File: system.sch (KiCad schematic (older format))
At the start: 23 parts, among them IC2 AM335X_ZCZ, P5 JTAG, U4 74LVC1G07DCK, Y1 24MHz, Y2 32.768kHz MC-306

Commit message: add display connector, bom generated, sch second version
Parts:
- added L11: BLM15AG102SN1D, symbol L
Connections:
- net labels added: CLKOUT1
- wire segments 61 -> 62
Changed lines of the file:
@@
 JTAG_EMU1
 Wire Wire Line
-	5725 4275 6200 4275
+	5725 4275 6350 4275
 Text Label 6200 4275 2    60   ~ 0
 JTAG_EMU2
@@
 P 5725 4575
 F 0 "W2" V 5725 4800 50  0000 C CNN
-F 1 "TESTOUT" V 5725 5075 50  0000 C CNN
+F 1 "TESTOUT" V 5800 4900 50  0000 C CNN
 F 2 "" H 5925 4575 50  0000 C CNN
 F 3 "" H 5925 4575 50  0000 C CNN
@@
 U 1 1 58B9CB53
 P 6500 4375
-F 0 "L8" V 6450 4375 50  0000 C CNN
-F 1 "BLM15AG102SN1D" V 6575 4375 50  0000 C CNN
+F 0 "L8" V 6575 4375 50  0000 C CNN
+F 1 "BLM15AG102SN1D" V 6650 4375 50  0000 C CNN
 F 2 "" H 6500 4375 50  0001 C CNN
 F 3 "" H 6500 4375 50  0001 C CNN
@@
 Wire Wire Line
 	6900 4375 6650 4375
+Text HLabel 6900 4275 2    60   Output ~ 0
+CLKOUT1
+$Comp
+L L L11
+U 1 1 58CCCA16
+P 6500 4275
+F 0 "L11" V 6375 4275 50  0000 C CNN
+F 1 "BLM15AG102SN1D" V 6450 4325 50  0000 C CNN
+F 2 "" H 6500 4275 50  0001 C CNN
+F 3 "" H 6500 4275 50  0001 C CNN
+	1    6500 4275
+	0    1    1    0
+$EndComp
+Wire Wire Line
+	6650 4275 6900 4275
 $EndSCHEMATC

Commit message: wip bom, fix some capacitors
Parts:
- C116, C117: value 100nF/10V -> 100nF/6.3V
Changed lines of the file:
@@
 P 2400 6300
 F 0 "C116" H 2425 6400 50  0000 L CNN
-F 1 "100nF/10V" H 2425 6200 50  0000 L CNN
+F 1 "100nF/6.3V" H 2425 6200 50  0000 L CNN
 F 2 "" H 2438 6150 50  0000 C CNN
 F 3 "" H 2400 6300 50  0000 C CNN
@@
 P 3325 6550
 F 0 "C117" H 3350 6650 50  0000 L CNN
-F 1 "100nF/10V" H 3350 6450 50  0000 L CNN
+F 1 "100nF/6.3V" H 3350 6450 50  0000 L CNN
 F 2 "" H 3363 6400 50  0000 C CNN
 F 3 "" H 3325 6550 50  0000 C CNN

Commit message: wip sch
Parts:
- removed C120, C121: 18pF/50V, symbol C
- removed IC2: AM335X_ZCZ, symbol AM335X_ZCZ
- removed Y2: 32.768kHz MC-306, symbol Crystal_GND23
- added C? (x2): 18pF/50V, symbol C
- added C?: 2.2uF/6.3V, symbol C
- added C?: 100nF/6.3V, symbol C
- added D? (x4): LTST-C191TBKT, symbol LED
- added IC?: OSD335x, GHI-SoMs-Processors_OSD3358, symbol OSD335x
- added IC?: NAND_4GB, footprints:WFBGA153, symbol NAND_4GB
- added P?: microSD, symbol microSD
- added R?: DNP 1M, symbol R
- added R? (x4): 1k, symbol R
- added R? (x18): 10k, symbol R
- added R?: 0R, symbol R
- added U?: SN74LVC1G06DCK, symbol 74AHC1G14
- added Y?: 32.768kHz, symbol Crystal
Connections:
- net labels added: GNDSHIELD, MMC1_CLK, MMC1_CMD, MMC1_DAT0, MMC1_DAT1, MMC1_DAT2, MMC1_DAT3, MMC1_DAT4, MMC1_DAT5, MMC1_DAT6, MMC1_DAT7, SD.CD, SD.CLK, SD.CMD, SD.D0, SD.D1, SD.D2, SD.D3, TIMER4, TIMER5, TIMER6, TIMER7, USR0, USR1, USR2, USR3, eHRPWM1A, eHRPWM1B, eHRPWM2A, eHRPWM2B, eMMC_RSTn
- net labels removed: GND_OSC, VSS_RTC
- wire segments 62 -> 254
- no-connect marks 3 -> 1
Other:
- moved on the sheet: C116, C117, C118, C119, C122, L11, L8, R32, R33, R34, R35, R36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

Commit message: wip sys and power
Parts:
- removed C116, C117: 100nF/6.3V, symbol C
- removed D? (x4): LTST-C191TBKT, symbol LED
- removed L11: BLM15AG102SN1D, symbol L
- removed P5: JTAG, symbol CONN_02X10
- removed P?: microSD, symbol microSD
- removed R32, R33, R34, R35: 4.75k, symbol R
- removed R37: 0R, symbol R
- removed R38, R? (x7): 10k, symbol R
- removed R? (x4): 1k, symbol R
- removed S2: Reset Button, symbol PushButton
- removed W2: TESTOUT, symbol TEST_1P
- added C? (x3): 100nF/6.3V, symbol C
- added C? (x3): 2.2uF/6.3V, symbol C
- added L?: BLM15AG102SN1D, symbol L
- added R?: 0 1%, symbol R
- added R?: 0R, symbol R
- C122: value 2.2uF/10V -> 2.2uF/6.3V
- C?: value 2.2uF/6.3V -> 4.7uF/6.3V
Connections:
- net labels added: GPIO0_26, GPIO0_27, GPIO1_12, GPIO1_13, GPIO1_14, GPIO1_15, GPIO1_16, GPIO1_25, GPIO1_28, GPIO1_29, GPIO2_0, GPIO2_1, LDO_PGOOD, PMIC_INT, PMIC_PGOOD, PMIC_nWAKEUP, UART4_RXD, UART4_TXD, USB1_OCn, VDD_1V8
- net labels removed: GNDSHIELD, GPIO0_7, JTAG_EMU2, JTAG_EMU3, JTAG_EMU4, NMIn, PMIC_POWER_EN, POR, RTC_POR, VIO, VRTC, WAKEUP
- wire segments 254 -> 151
- no-connect marks 1 -> 0
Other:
- moved on the sheet: C122, C?, IC?, L8, R39, R?, U4, U?

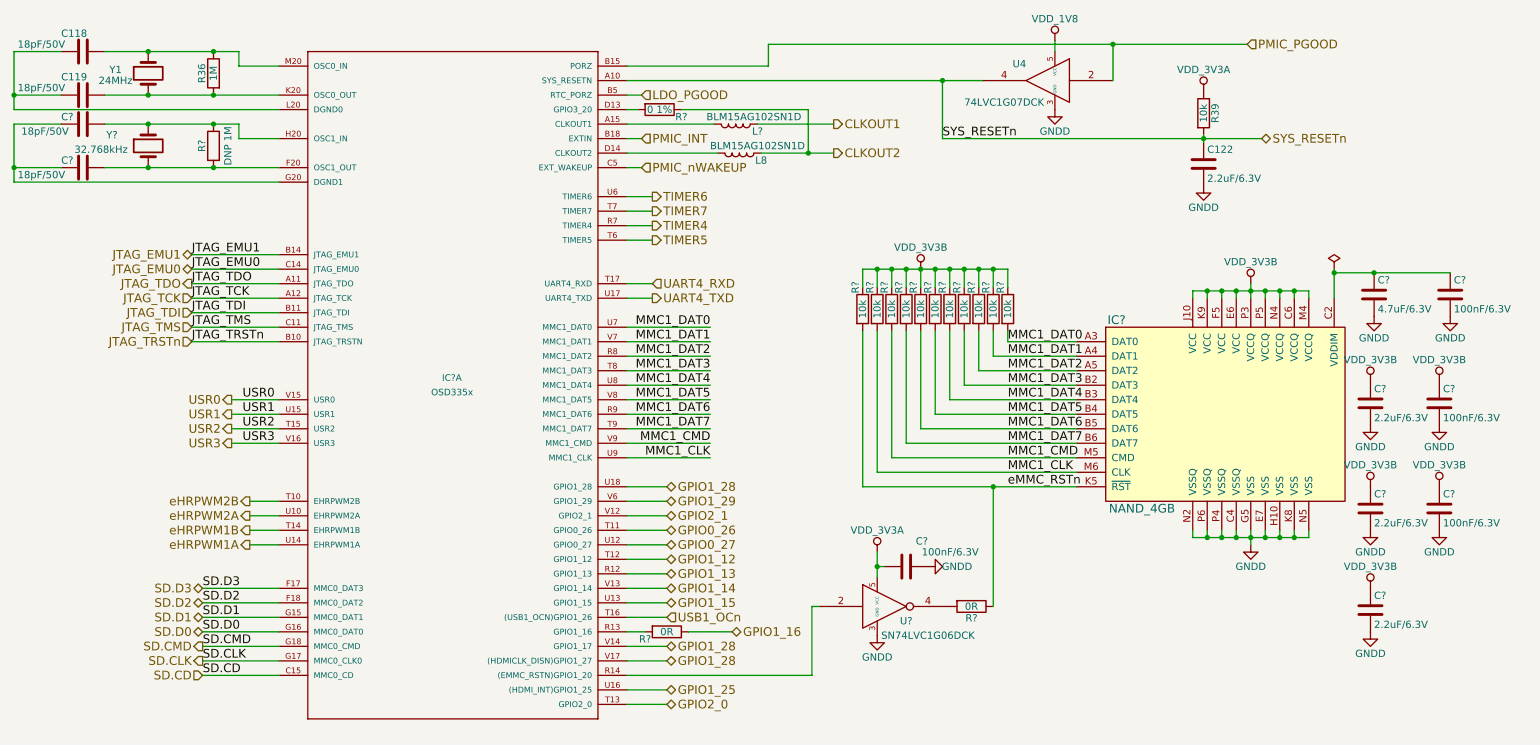
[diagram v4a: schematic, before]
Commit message: only io connectors remaining
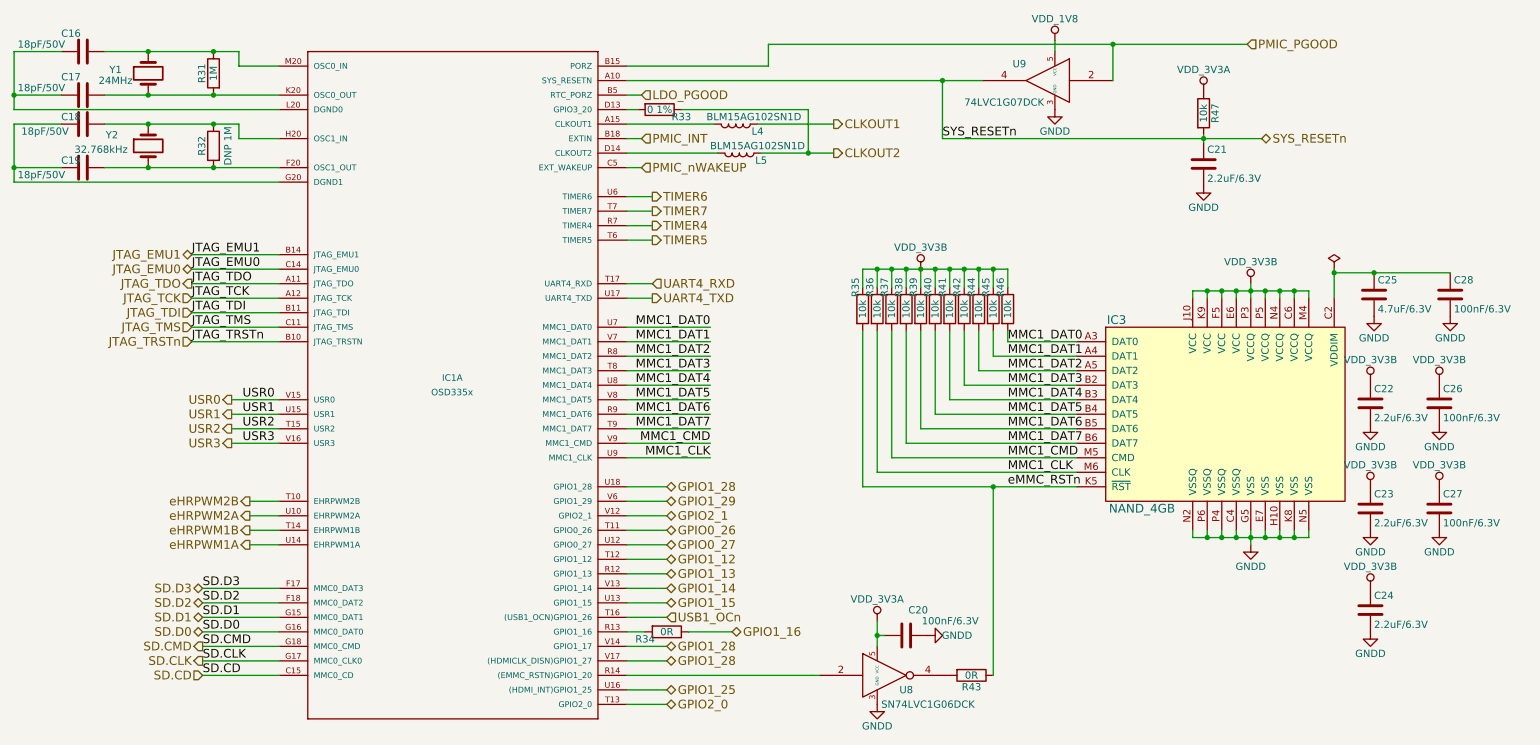
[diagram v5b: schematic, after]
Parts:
- gave numbers to parts that had none: 30
- renumbered C118 to C16, C119 to C17, C122 to C21, L8 to L5, R36 to R31, R39 to R47, U4 to U9
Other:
- moved on the sheet: C20, R43, U8

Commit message: wip erc
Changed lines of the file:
@@
 $EndComp
 Wire Wire Line
-	1375 775  1675 775
-Wire Wire Line
-	1675 775  2125 775
-Wire Wire Line
-	2125 775  2300 775
-Wire Wire Line
-	1375 1075 1675 1075
-Wire Wire Line
-	1675 1075 2125 1075
-Wire Wire Line
-	2125 1075 2575 1075
+	1375 775  2300 775
+Wire Wire Line
+	1375 1075 2575 1075
 $Comp
 L R R31
@@
 	1075 775  750  775
 Wire Wire Line
-	750  775  750  1075
-Wire Wire Line
-	750  1075 750  1175
+	750  775  750  1175
 Wire Wire Line
 	750  1075 1075 1075
@@
 $EndComp
 Wire Wire Line
-	5950 725  8325 725
-Wire Wire Line
-	8325 725  9250 725
+	5950 725  9250 725
 Text HLabel 9250 725  2    60   Input ~ 0
 PMIC_PGOOD
@@
 $EndComp
 Wire Wire Line
-	4975 975  7150 975
-Wire Wire Line
-	7150 975  7425 975
+	4975 975  7425 975
 $Comp
 L GNDD #PWR75
@@
 Connection ~ 8325 725
 Wire Wire Line
-	7150 1375 8950 1375
-Wire Wire Line
-	8950 1375 9350 1375
+	7150 1375 9350 1375
 Wire Wire Line
 	7150 1375 7150 975
@@
 $EndComp
 Wire Wire Line
-	8950 1350 8950 1375
-Wire Wire Line
-	8950 1375 8950 1400
+	8950 1350 8950 1400
 Connection ~ 8950 1375
 $Comp
@@
 CLKOUT2
 Wire Wire Line
-	5900 1475 6225 1475
-Wire Wire Line
-	6225 1475 6400 1475
+	5900 1475 6400 1475
 $Comp
 L OSD335x IC1
@@
 $EndComp
 Wire Wire Line
-	1375 1275 1675 1275
-Wire Wire Line
-	1675 1275 2125 1275
-Wire Wire Line
-	2125 1275 2300 1275
-Wire Wire Line
-	1375 1575 1675 1575
-Wire Wire Line
-	1675 1575 2125 1575
-Wire Wire Line
-	2125 1575 2575 1575
+	1375 1275 2300 1275
+Wire Wire Line
+	1375 1575 2575 1575
 $Comp
 L R R32
@@
 	1075 1275 750  1275
 Wire Wire Line
-	750  1275 750  1575
-Wire Wire Line
-	750  1575 750  1675
+	750  1275 750  1675
 Wire Wire Line
 	750  1575 1075 1575
@@
 Connection ~ 9175 2425
 Wire Wire Line
-	9275 2375 9275 2425
-Wire Wire Line
-	9275 2425 9275 2475
+	9275 2375 9275 2475
 Connection ~ 9275 2425
 Wire Wire Line
@@
 	9675 2425 9675 2475
 Wire Wire Line
-	8875 2425 8975 2425
-Wire Wire Line
-	8975 2425 9075 2425
-Wire Wire Line
-	9075 2425 9175 2425
-Wire Wire Line
-	9175 2425 9275 2425
-Wire Wire Line
-	9275 2425 9375 2425
-Wire Wire Line
-	9375 2425 9475 2425
-Wire Wire Line
-	9475 2425 9575 2425
-Wire Wire Line
-	9575 2425 9675 2425
+	8875 2425 9675 2425
 $Comp
 L C C25
@@
 $EndComp
 Wire Wire Line
-	9850 2275 9850 2300
-Wire Wire Line
-	9850 2300 9850 2475
-Wire Wire Line
-	9850 2300 10125 2300
-Wire Wire Line
-	10125 2300 10650 2300
+	9850 2275 9850 2475
+Wire Wire Line
+	9850 2300 10650 2300
 $Comp
 L GNDD #PWR79
@@
 Connection ~ 9175 4125
 Wire Wire Line
-	9275 4075 9275 4125
-Wire Wire Line
-	9275 4125 9275 4175
+	9275 4075 9275 4175
 Connection ~ 9275 4125
 Wire Wire Line
@@
 	9675 4125 9675 4075
 Wire Wire Line
-	8875 4125 8975 4125
-Wire Wire Line
-	8975 4125 9075 4125
-Wire Wire Line
-	9075 4125 9175 4125
-Wire Wire Line
-	9175 4125 9275 4125
-Wire Wire Line
-	9275 4125 9375 4125
-Wire Wire Line
-	9375 4125 9475 4125
-Wire Wire Line
-	9475 4125 9575 4125
-Wire Wire Line
-	9575 4125 9675 4125
+	8875 4125 9675 4125
 $Comp
 L R R42
@@
 Connection ~ 6900 2275
 Wire Wire Line
-	6600 2275 6700 2275
-Wire Wire Line
-	6700 2275 6800 2275
-Wire Wire Line
-	6800 2275 6900 2275
-Wire Wire Line
-	6900 2275 7000 2275
-Wire Wire Line
-	7000 2275 7100 2275
-Wire Wire Line
-	7100 2275 7200 2275
-Wire Wire Line
-	7200 2275 7300 2275
-Wire Wire Line
-	7300 2275 7400 2275
-Wire Wire Line
-	7400 2275 7500 2275
-Wire Wire Line
-	7500 2275 7600 2275
+	6600 2275 7600 2275
 Wire Wire Line
 	7000 2275 7000 2400
@@
 	6600 2700 6600 3775
 Wire Wire Line
-	6600 3775 7500 3775
-Wire Wire Line
-	7500 3775 8075 3775
+	6600 3775 8075 3775
 Text Label 7600 2775 0    60   ~ 0
 MMC1_DAT0
@@
 	6750 4800 6700 4800
 Wire Wire Line
-	6700 4700 6700 4800
-Wire Wire Line
-	6700 4800 6700 4875
+	6700 4700 6700 4875
 Connection ~ 6700 4800
 Wire Wire Line
@@
 $EndComp
 Wire Wire Line
-	4975 5075 6250 5075
-Wire Wire Line
-	6250 5075 6250 5075
-Wire Wire Line
-	6250 5075 6300 5075
+	4975 5075 6300 5075
 Wire Wire Line
 	4975 3775 5250 3775

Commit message: erc passed
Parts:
- IC1: symbol OSD335x -> OSD335x-RESCUE-mateboard
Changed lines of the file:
@@
 	4975 975  7425 975
 $Comp
-L GNDD #PWR75
+L GNDD #PWR0106
 U 1 1 58AFE459
 P 7925 1175
-F 0 "#PWR75" H 7925 925 50  0001 C CNN
+F 0 "#PWR0106" H 7925 925 50  0001 C CNN
 F 1 "GNDD" H 7925 1025 50  0000 C CNN
 F 2 "" H 7925 1175 50  0000 C CNN
@@
 Connection ~ 8950 1375
 $Comp
-L VDD_3V3A #PWR76
+L VDD_3V3A #PWR0107
 U 1 1 58AFF28A
 P 8950 1050
-F 0 "#PWR76" H 8950 900 50  0001 C CNN
+F 0 "#PWR0107" H 8950 900 50  0001 C CNN
 F 1 "VDD_3V3A" H 8950 1200 50  0000 C CNN
 F 2 "" H 8950 1050 50  0000 C CNN
@@
 $EndComp
 $Comp
-L GNDD #PWR77
+L GNDD #PWR0108
 U 1 1 58AFF2DD
 P 8950 1700
-F 0 "#PWR77" H 8950 1450 50  0001 C CNN
+F 0 "#PWR0108" H 8950 1450 50  0001 C CNN
 F 1 "GNDD" H 8950 1550 50  0000 C CNN
 F 2 "" H 8950 1700 50  0000 C CNN
@@
 	5900 1475 6400 1475
 $Comp
-L OSD335x IC1
+L OSD335x-RESCUE-mateboard IC1
 U 1 1 58D2CE56
 P 3775 3075
+AR Path="/58D2CE56" Ref="IC1"  Part="1"
+AR Path="/58AC1B74/58D2CE56" Ref="IC1"  Part="1"
 F 0 "IC1" H 3700 3100 45  0000 L BNN
 F 1 "OSD335x" H 3625 3000 45  0000 L BNN
@@
 $EndComp
 $Comp
-L VDD_3V3B #PWR78
+L VDD_3V3B #PWR0109
 U 1 1 58D48CDC
 P 9275 2375
-F 0 "#PWR78" H 9275 2225 50  0001 C CNN
+F 0 "#PWR0109" H 9275 2225 50  0001 C CNN
 F 1 "VDD_3V3B" H 9275 2525 50  0000 C CNN
 F 2 "" H 9275 2375 50  0000 C CNN
@@
 $EndComp
 $Comp
-L GNDD #PWR86
+L GNDD #PWR0110
 U 1 1 58D48CFA
 P 10125 2600
-F 0 "#PWR86" H 10125 2350 50  0001 C CNN
+F 0 "#PWR0110" H 10125 2350 50  0001 C CNN
 F 1 "GNDD" H 10125 2450 50  0000 C CNN
 F 2 "" H 10125 2600 50  0000 C CNN
@@
 	9850 2300 10650 2300
 $Comp
-L GNDD #PWR79
+L GNDD #PWR0111
 U 1 1 58D48D02
 P 9275 4175
-F 0 "#PWR79" H 9275 3925 50  0001 C CNN
+F 0 "#PWR0111" H 9275 3925 50  0001 C CNN
 F 1 "GNDD" H 9275 4025 50  0000 C CNN
 F 2 "" H 9275 4175 50  0000 C CNN
@@
 $EndComp
 $Comp
-L VDD_3V3B #PWR72
+L VDD_3V3B #PWR0112
 U 1 1 58D48D66
 P 7000 2275
-F 0 "#PWR72" H 7000 2125 50  0001 C CNN
+F 0 "#PWR0112" H 7000 2125 50  0001 C CNN
 F 1 "VDD_3V3B" H 7000 2425 50  0000 C CNN
 F 2 "" H 7000 2275 50  0000 C CNN
@@
 $EndComp
 $Comp
-L VDD_3V3A #PWR70
+L VDD_3V3A #PWR0113
 U 1 1 58D48DB0
 P 6700 4700
-F 0 "#PWR70" H 6700 4550 50  0001 C CNN
+F 0 "#PWR0113" H 6700 4550 50  0001 C CNN
 F 1 "VDD_3V3A" H 6700 4850 50  0000 C CNN
 F 2 "" H 6700 4700 50  0000 C CNN
@@
 $EndComp
 $Comp
-L GNDD #PWR71
+L GNDD #PWR0114
 U 1 1 58D48DB6
 P 6700 5275
-F 0 "#PWR71" H 6700 5025 50  0001 C CNN
+F 0 "#PWR0114" H 6700 5025 50  0001 C CNN
 F 1 "GNDD" H 6700 5125 50  0000 C CNN
 F 2 "" H 6700 5275 50  0000 C CNN
@@
 $EndComp
 $Comp
-L GNDD #PWR73
+L GNDD #PWR0115
 U 1 1 58D48DC3
 P 7050 4800
-F 0 "#PWR73" H 7050 4550 50  0001 C CNN
+F 0 "#PWR0115" H 7050 4550 50  0001 C CNN
 F 1 "GNDD" V 7050 4600 50  0000 C CNN
 F 2 "" H 7050 4800 50  0000 C CNN
@@
 Connection ~ 7500 3775
 $Comp
-L PWR_FLAG #FLG3
+L PWR_FLAG #FLG0116
 U 1 1 58D48DD0
 P 9850 2275
-F 0 "#FLG3" H 9850 2350 50  0001 C CNN
+F 0 "#FLG0116" H 9850 2350 50  0001 C CNN
 F 1 "PWR_FLAG" H 9850 2425 50  0001 C CNN
 F 2 "" H 9850 2275 50  0001 C CNN
@@
 	5950 875  4975 875
 $Comp
-L VDD_1V8 #PWR74
+L VDD_1V8 #PWR0117
 U 1 1 58DA59D5
 P 7925 700
-F 0 "#PWR74" H 7925 550 50  0001 C CNN
+F 0 "#PWR0117" H 7925 550 50  0001 C CNN
 F 1 "VDD_1V8" H 7925 850 50  0000 C CNN
 F 2 "" H 7925 700 50  0000 C CNN
@@
 $EndComp
 $Comp
-L GNDD #PWR91
+L GNDD #PWR0118
 U 1 1 58DADD35
 P 10650 2600
-F 0 "#PWR91" H 10650 2350 50  0001 C CNN
+F 0 "#PWR0118" H 10650 2350 50  0001 C CNN
 F 1 "GNDD" H 10650 2450 50  0000 C CNN
 F 2 "" H 10650 2600 50  0000 C CNN
@@
 $EndComp
 $Comp
-L GNDD #PWR81
+L GNDD #PWR0119
 U 1 1 58DAEBBD
 P 10100 3350
-F 0 "#PWR81" H 10100 3100 50  0001 C CNN
+F 0 "#PWR0119" H 10100 3100 50  0001 C CNN
 F 1 "GNDD" H 10100 3200 50  0000 C CNN
 F 2 "" H 10100 3350 50  0000 C CNN
@@
 $EndComp
 $Comp
-L GNDD #PWR88
+L GNDD #PWR0120
 U 1 1 58DAEC64
 P 10575 3350
-F 0 "#PWR88" H 10575 3100 50  0001 C CNN
+F 0 "#PWR0120" H 10575 3100 50  0001 C CNN
 F 1 "GNDD" H 10575 3200 50  0000 C CNN
 F 2 "" H 10575 3350 50  0000 C CNN
@@
 	5400 4775 5700 4775
 $Comp
-L VDD_3V3B #PWR80
+L VDD_3V3B #PWR0121
 U 1 1 58DB0C91
 P 10100 3050
-F 0 "#PWR80" H 10100 2900 50  0001 C CNN
+F 0 "#PWR0121" H 10100 2900 50  0001 C CNN
 F 1 "VDD_3V3B" H 10100 3200 50  0000 C CNN
 F 2 "" H 10100 3050 50  0000 C CNN
@@
 $EndComp
 $Comp
-L VDD_3V3B #PWR87
+L VDD_3V3B #PWR0122
 U 1 1 58DB0D28
 P 10575 3050
-F 0 "#PWR87" H 10575 2900 50  0001 C CNN
+F 0 "#PWR0122" H 10575 2900 50  0001 C CNN
 F 1 "VDD_3V3B" H 10575 3200 50  0000 C CNN
 F 2 "" H 10575 3050 50  0000 C CNN
@@
 $EndComp
 $Comp
-L GNDD #PWR83
+L GNDD #PWR0123
 U 1 1 58DB0E3C
 P 10100 4075
-F 0 "#PWR83" H 10100 3825 50  0001 C CNN
+F 0 "#PWR0123" H 10100 3825 50  0001 C CNN
 F 1 "GNDD" H 10100 3925 50  0000 C CNN
 F 2 "" H 10100 4075 50  0000 C CNN
@@
 $EndComp
 $Comp
-L VDD_3V3B #PWR82
+L VDD_3V3B #PWR0124
 U 1 1 58DB0E42
 P 10100 3775
-F 0 "#PWR82" H 10100 3625 50  0001 C CNN
+F 0 "#PWR0124" H 10100 3625 50  0001 C CNN
 F 1 "VDD_3V3B" H 10100 3925 50  0000 C CNN
 F 2 "" H 10100 3775 50  0000 C CNN
@@
 $EndComp
 $Comp
-L GNDD #PWR85
+L GNDD #PWR0125
 U 1 1 58DB0EE7
 P 10100 4775
-F 0 "#PWR85" H 10100 4525 50  0001 C CNN
+F 0 "#PWR0125" H 10100 4525 50  0001 C CNN
 F 1 "GNDD" H 10100 4625 50  0000 C CNN
 F 2 "" H 10100 4775 50  0000 C CNN
@@
 $EndComp
 $Comp
-L VDD_3V3B #PWR84
+L VDD_3V3B #PWR0126
 U 1 1 58DB0EED
 P 10100 4475
-F 0 "#PWR84" H 10100 4325 50  0001 C CNN
+F 0 "#PWR0126" H 10100 4325 50  0001 C CNN
 F 1 "VDD_3V3B" H 10100 4625 50  0000 C CNN
 F 2 "" H 10100 4475 50  0000 C CNN
@@
 $EndComp
 $Comp
-L GNDD #PWR90
+L GNDD #PWR0127
 U 1 1 58DB11F2
 P 10575 4075
-F 0 "#PWR90" H 10575 3825 50  0001 C CNN
+F 0 "#PWR0127" H 10575 3825 50  0001 C CNN
 F 1 "GNDD" H 10575 3925 50  0000 C CNN
 F 2 "" H 10575 4075 50  0000 C CNN
@@
 $EndComp
 $Comp
-L VDD_3V3B #PWR89
+L VDD_3V3B #PWR0128
 U 1 1 58DB11F8
 P 10575 3775
-F 0 "#PWR89" H 10575 3625 50  0001 C CNN
+F 0 "#PWR0128" H 10575 3625 50  0001 C CNN
 F 1 "VDD_3V3B" H 10575 3925 50  0000 C CNN
 F 2 "" H 10575 3775 50  0000 C CNN
